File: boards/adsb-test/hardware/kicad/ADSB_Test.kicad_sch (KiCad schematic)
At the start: 0 parts

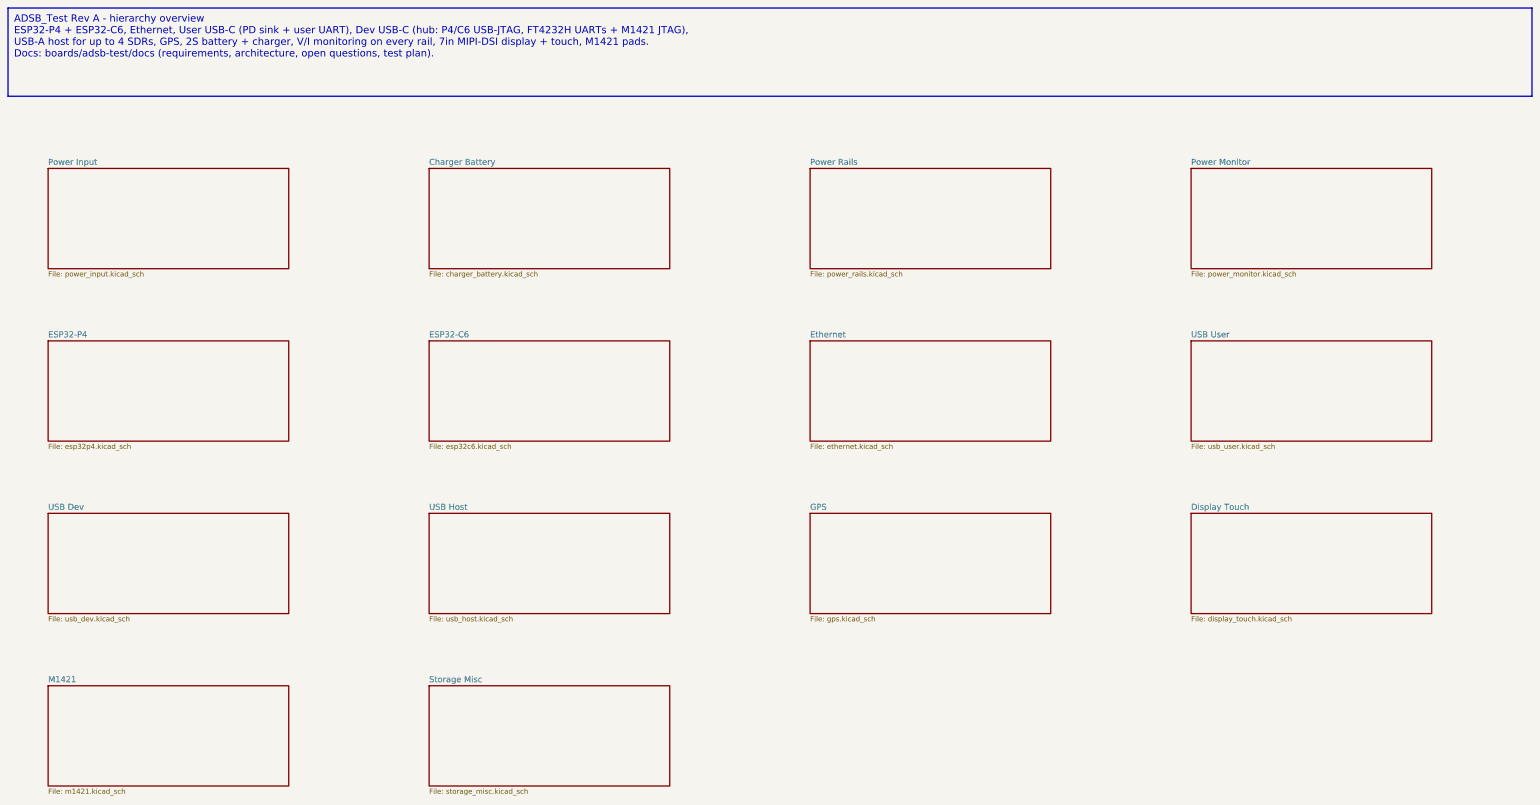
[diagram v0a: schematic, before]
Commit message: Release v0.4.0: ADSB_Test with ESP32-C5, ADSBee m1421 and LA5016 header
- C6 -> C5 co-processor; m1421 identified and integrated (symbol/footprint
  from the ADSBee 1421 carrier, GPL-3.0 attribution)
- Power budget and 2S1P battery sizing for >= 1 h; USB-A for 1-2 SDRs via hub
- Dev port: FT2232H + RP2040 debugprobe; TCA6408A expander for slow I/O
- Test Debug sheet with LA5016 header and rail test points
- Vendor documents git-ignored (public repo)

Co-Authored-By: Claude Opus 5.5 <noreply@anthropic.com>
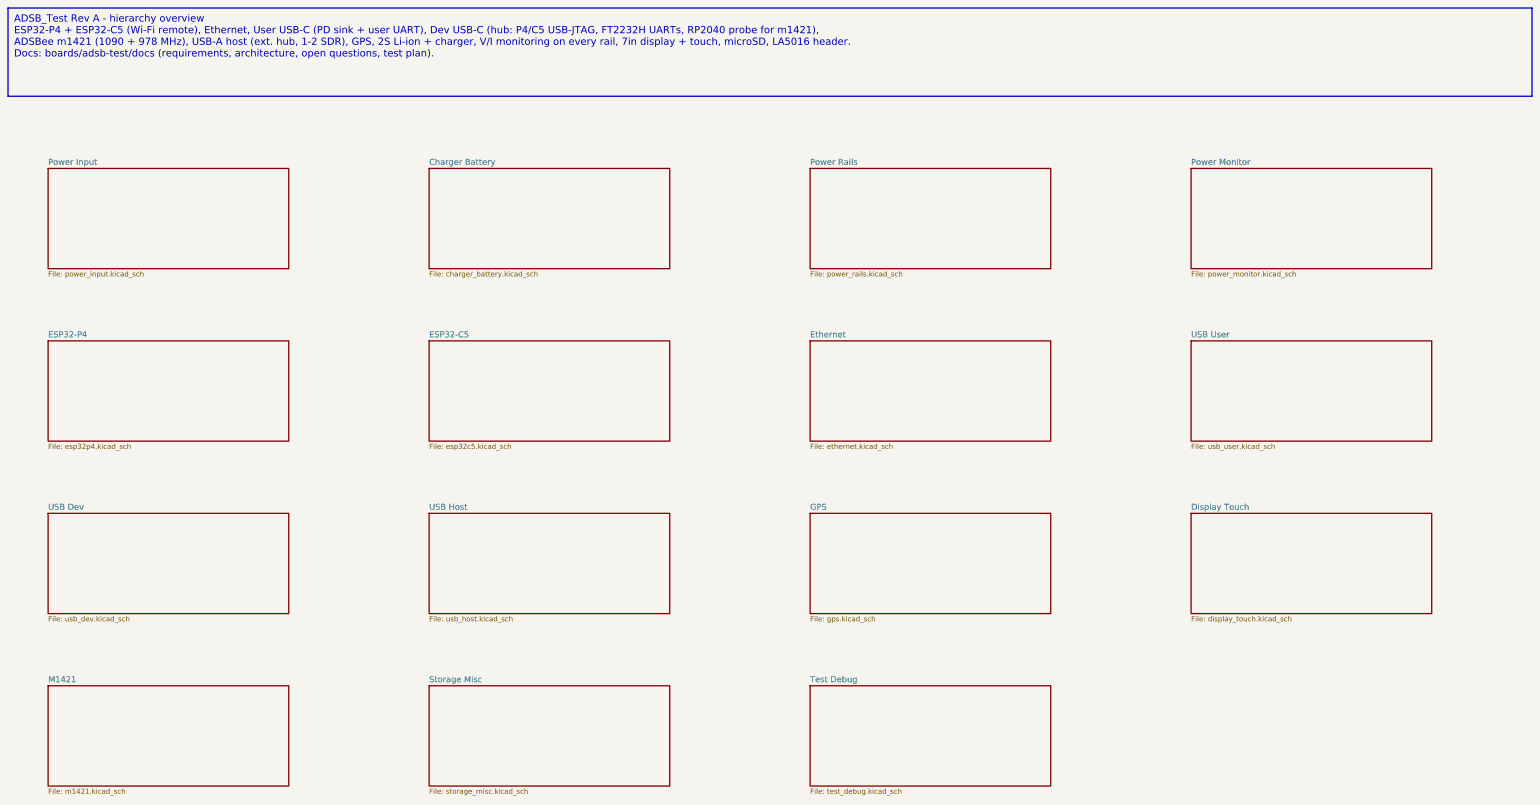
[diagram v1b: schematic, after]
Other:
- removed sheet ESP32-C6
- added sheet ESP32-C5 (esp32c5.kicad_sch)
- added sheet Test Debug (test_debug.kicad_sch)
